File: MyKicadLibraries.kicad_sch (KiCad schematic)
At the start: 23 parts, among them J1 Conn_01x08, J2 Conn_01x08, J3 POGO Pins, J4 c8-inlet, J5 FTDI, J6 Micro_SD_Card, SW1 Schurter Switch, U1 radio-receiver, U10 rdm-6300, U11 magnetic-charger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

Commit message: Update tp4056 footprint
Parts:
- gave numbers to parts that had none: 1
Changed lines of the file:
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@@
   (symbol (lib_id "ftdi-connector:TTL") (at 126.746 53.848 0) (unit 1)
     (in_bom yes) (on_board yes) (fields_autoplaced)
-    (property "Reference" "U?" (id 0) (at 133.604 53.8479 0)
+    (property "Reference" "U13" (id 0) (at 133.604 53.8479 0)
       (effects (font (size 1.27 1.27)) (justify left))
     )
@@
     )
     (path "/435d2a60-6fae-43fe-9627-fd91fed8fe4a"
-      (reference "U?") (unit 1) (value "TTL") (footprint "Connector_PinHeader_2.54mm:PinHeader_1x04_P2.54mm_Vertical")
-    )
-  )
+      (reference "U13") (unit 1) (value "TTL") (footprint "Connector_PinHeader_2.54mm:PinHeader_1x04_P2.54mm_Vertical")
+    )
+  )

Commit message: Add SOIC8 breakout
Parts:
- added J7, J9: Conn_01x04, Connector_PinHeader_2.54mm:PinHeader_1x04_P2.54mm_Vertical, symbol Connector_Generic:Conn_01x04
- added J8: Conn_02x04_Counter_Clockwise, Package_SO:SOIC-8_3.9x4.9mm_P1.27mm, symbol Connector_Generic:Conn_02x04_Counter_Clockwise
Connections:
- new net: J8.5 (Pin_5), J9.1 (Pin_1)
- new net: J8.6 (Pin_6), J9.2 (Pin_2)
- new net: J8.7 (Pin_7), J9.3 (Pin_3)
- new net: J8.8 (Pin_8), J9.4 (Pin_4)
- new net: J7.1 (Pin_1), J8.1 (Pin_1)
- new net: J7.2 (Pin_2), J8.2 (Pin_2)
- new net: J7.3 (Pin_3), J8.3 (Pin_3)
- new net: J7.4 (Pin_4), J8.4 (Pin_4)
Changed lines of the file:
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@@
+    (pin "4")
+  )
+  (symbol (lib_id "Connector_Generic:Conn_01x04") (at 260.604 29.21 0) (mirror x) (unit 1)
+    (in_bom yes) (on_board yes) (fields_autoplaced)
+    (property "Reference" "J9" (id 0) (at 260.604 20.32 0))
+    (property "Value" "Conn_01x04" (id 1) (at 260.604 20.574 0)
+      (effects (font (size 1.27 1.27)) hide)
+    )
+    (property "Footprint" "Connector_PinHeader_2.54mm:PinHeader_1x04_P2.54mm_Vertical" (id 2) (at 260.604 29.21 0)
+      (effects (font (size 1.27 1.27)) hide)
+    )
+    (property "Datasheet" "~" (id 3) (at 260.604 29.21 0)
+      (effects (font (size 1.27 1.27)) hide)
+    )
+    (pin "1")
+    (pin "2")
+    (pin "3")
+    (pin "4")
+  )
+  (symbol (lib_id "Connector_Generic:Conn_01x04") (at 237.744 26.67 0) (mirror y) (unit 1)
+    (in_bom yes) (on_board yes) (fields_autoplaced)
+    (property "Reference" "J7" (id 0) (at 237.744 20.32 0))
+    (property "Value" "Conn_01x04" (id 1) (at 237.744 20.32 0)
+      (effects (font (size 1.27 1.27)) hide)
+    )
+    (property "Footprint" "Connector_PinHeader_2.54mm:PinHeader_1x04_P2.54mm_Vertical" (id 2) (at 237.744 26.67 0)
+      (effects (font (size 1.27 1.27)) hide)
+    )
+    (property "Datasheet" "~" (id 3) (at 237.744 26.67 0)
+      (effects (font (size 1.27 1.27)) hide)
+    )
+    (pin "1")
+    (pin "2")
+    (pin "3")
     (pin "4")
   )
@@
     (pin "9")
   )
+  (symbol (lib_id "Connector_Generic:Conn_02x04_Counter_Clockwise") (at 247.904 26.67 0) (unit 1)
+    (in_bom yes) (on_board yes) (fields_autoplaced)
+    (property "Reference" "J8" (id 0) (at 249.174 17.78 0))
+    (property "Value" "Conn_02x04_Counter_Clockwise" (id 1) (at 249.174 20.32 0))
+    (property "Footprint" "Package_SO:SOIC-8_3.9x4.9mm_P1.27mm" (id 2) (at 247.904 26.67 0)
+      (effects (font (size 1.27 1.27)) hide)
+    )
+    (property "Datasheet" "~" (id 3) (at 247.904 26.67 0)
+      (effects (font (size 1.27 1.27)) hide)
+    )
+    (pin "1")
+    (pin "2")
+    (pin "3")
+    (pin "4")
+    (pin "5")
+    (pin "6")
+    (pin "7")
+    (pin "8")
+  )
   (symbol (lib_id "ESP8266:ESP-12E") (at 240.665 135.255 0) (unit 1)
     (in_bom yes) (on_board yes) (fields_autoplaced)
@@
       (reference "J6") (unit 1) (value "Micro_SD_Card") (footprint "sd-card:sd-card")
     )
+    (path "/c7e9b8b9-307f-4e5a-a9a6-364a90b8e346"
+      (reference "J7") (unit 1) (value "Conn_01x04") (footprint "Connector_PinHeader_2.54mm:PinHeader_1x04_P2.54mm_Vertical")
+    )
+    (path "/d1d3df4c-041c-4333-92a6-361f8f8487b4"
+      (reference "J8") (unit 1) (value "Conn_02x04_Counter_Clockwise") (footprint "Package_SO:SOIC-8_3.9x4.9mm_P1.27mm")
+    )
+    (path "/c112f6ba-1a8d-4939-9e1a-222f084633ca"
+      (reference "J9") (unit 1) (value "Conn_01x04") (footprint "Connector_PinHeader_2.54mm:PinHeader_1x04_P2.54mm_Vertical")
+    )
     (path "/93625391-d5f1-4afc-86f7-69a3da3b5437"

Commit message: Add rcj-22 plug as well as lxb18 module
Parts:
- added J10: RCJ-22, rcj-22:rcj-22, symbol rcj-22:RCJ-22
- added U14: lxb18, lxb18:lxb18, symbol lxb18:lxb18
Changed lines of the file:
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@@
     (pin "7")
+  )
+  (symbol (lib_id "rcj-22:RCJ-22") (at 164.592 132.08 0) (unit 1)
+    (in_bom yes) (on_board yes) (fields_autoplaced)
+    (property "Reference" "J10" (id 0) (at 163.0045 121.92 0))
+    (property "Value" "RCJ-22" (id 1) (at 163.0045 124.46 0))
+    (property "Footprint" "rcj-22:rcj-22" (id 2) (at 162.687 140.97 0)
+      (effects (font (size 1.27 1.27)) (justify bottom) hide)
+    )
+    (property "Datasheet" "" (id 3) (at 179.832 142.24 0)
+      (effects (font (size 1.27 1.27)) hide)
+    )
+    (pin "1")
+    (pin "2")
+    (pin "3")
   )
   (symbol (lib_id "adafruit-MAX98357:adafruit-MAX98357") (at 94.234 116.586 0) (unit 1)
@@
     (pin "1")
     (pin "2")
+  )
+  (symbol (lib_id "lxb18:lxb18") (at 247.396 75.438 0) (unit 1)
+    (in_bom yes) (on_board yes)
+    (property "Reference" "U14" (id 0) (at 240.03 66.548 0)
+      (effects (font (size 1.27 1.27)) (justify left))
+    )
+    (property "Value" "lxb18" (id 1) (at 250.698 84.328 0)
+      (effects (font (size 1.27 1.27)) (justify left))
+    )
+    (property "Footprint" "lxb18:lxb18" (id 2) (at 242.316 75.438 0)
+      (effects (font (size 1.27 1.27)) hide)
+    )
+    (property "Datasheet" "" (id 3) (at 242.316 75.438 0)
+      (effects (font (size 1.27 1.27)) hide)
+    )
+    (pin "1")
+    (pin "2")
+    (pin "3")
+    (pin "4")
+    (pin "5")
+    (pin "6")
+    (pin "7")
+    (pin "8")
   )
   (symbol (lib_id "c8-inlet:c8-inlet") (at 94.234 77.978 0) (unit 1)
@@
       (reference "J9") (unit 1) (value "Conn_01x04") (footprint "Connector_PinHeader_2.54mm:PinHeader_1x04_P2.54mm_Vertical")
     )
+    (path "/4e8a5cd3-7bbd-43a2-b3b1-8113fc79bbd5"
+      (reference "J10") (unit 1) (value "RCJ-22") (footprint "rcj-22:rcj-22")
+    )
     (path "/93625391-d5f1-4afc-86f7-69a3da3b5437"
       (reference "LIN1") (unit 1) (value "LEDs_In") (footprint "neopixel-strip:neopixel-strip")
@@
       (reference "U13") (unit 1) (value "TTL") (footprint "Connector_PinHeader_2.54mm:PinHeader_1x04_P2.54mm_Vertical")
     )
-  )
+    (path "/6cf58933-bb3e-42e1-bf60-7634f8d5f4b4"
+      (reference "U14") (unit 1) (value "lxb18") (footprint "lxb18:lxb18")
+    )
+  )

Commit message: Add midi connector
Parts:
- added J11: DIN-5, midi:midi, symbol Connector:DIN-5
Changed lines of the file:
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@@
     (pin "2")
+  )
+  (symbol (lib_id "Connector:DIN-5") (at 158.75 97.79 0) (unit 1)
+    (in_bom yes) (on_board yes) (fields_autoplaced)
+    (property "Reference" "J11" (id 0) (at 158.7501 105.41 0))
+    (property "Value" "DIN-5" (id 1) (at 158.7501 107.95 0))
+    (property "Footprint" "midi:midi" (id 2) (at 158.75 97.79 0)
+      (effects (font (size 1.27 1.27)) hide)
+    )
+    (property "Datasheet" "http://www.mouser.com/ds/2/18/40_c091_abd_e-75918.pdf" (id 3) (at 158.75 97.79 0)
+      (effects (font (size 1.27 1.27)) hide)
+    )
+    (pin "1")
+    (pin "2")
+    (pin "3")
+    (pin "4")
+    (pin "5")
   )
   (symbol (lib_id "ftdi-connector:FTDI") (at 108.204 54.61 0) (unit 1)
@@
       (reference "J10") (unit 1) (value "RCJ-22") (footprint "rcj-22:rcj-22")
     )
+    (path "/13dd7a5b-3ad4-40e9-9df7-e158c8bd37e9"
+      (reference "J11") (unit 1) (value "DIN-5") (footprint "midi:midi")
+    )
     (path "/93625391-d5f1-4afc-86f7-69a3da3b5437"

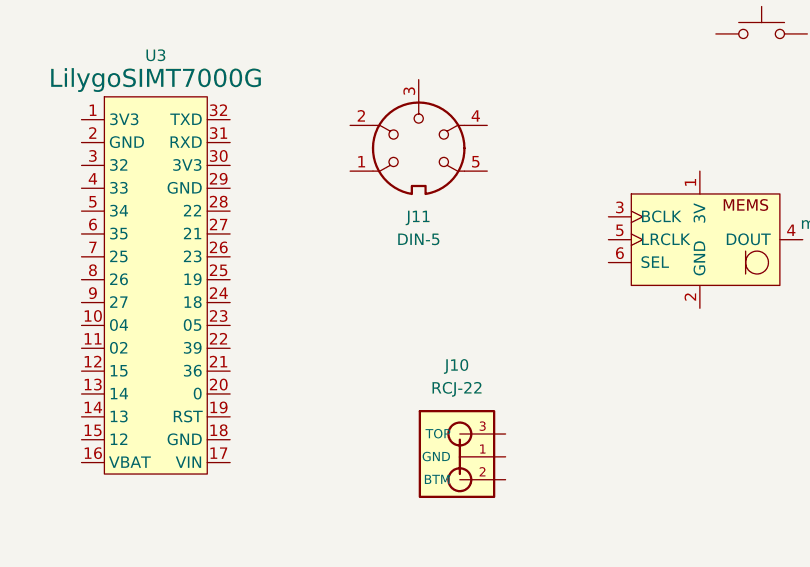
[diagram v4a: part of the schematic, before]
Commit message: Add din6 midi plug
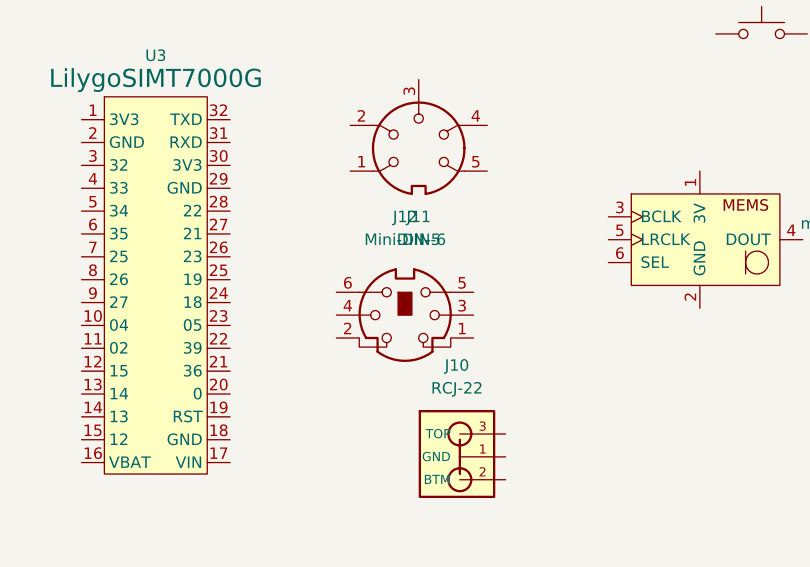
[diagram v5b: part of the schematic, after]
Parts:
- added J12: Mini-DIN-6, midi:midi-din6, symbol Connector:Mini-DIN-6
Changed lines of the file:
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@@
     (pin "THERMAL")
+  )
+  (symbol (lib_id "Connector:Mini-DIN-6") (at 157.226 116.332 0) (unit 1)
+    (in_bom yes) (on_board yes) (fields_autoplaced)
+    (property "Reference" "J12" (id 0) (at 157.2437 105.41 0))
+    (property "Value" "Mini-DIN-6" (id 1) (at 157.2437 107.95 0))
+    (property "Footprint" "midi:midi-din6" (id 2) (at 157.226 116.332 0)
+      (effects (font (size 1.27 1.27)) hide)
+    )
+    (property "Datasheet" "http://service.powerdynamics.com/ec/Catalog17/Section%2011.pdf" (id 3) (at 157.226 116.332 0)
+      (effects (font (size 1.27 1.27)) hide)
+    )
+    (pin "1")
+    (pin "2")
+    (pin "3")
+    (pin "4")
+    (pin "5")
+    (pin "6")
   )
   (symbol (lib_id "Switch:SW_Push") (at 196.85 85.09 0) (unit 1)
@@
       (reference "J11") (unit 1) (value "DIN-5") (footprint "midi:midi")
     )
+    (path "/62ed3167-06a5-430d-adba-50010e067d40"
+      (reference "J12") (unit 1) (value "Mini-DIN-6") (footprint "midi:midi-din6")
+    )
     (path "/93625391-d5f1-4afc-86f7-69a3da3b5437"

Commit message: Update submodules
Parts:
- added U15: esp32-wemos-d1-mini, esp32-wemos-d1-mini:esp32-wemos-d1-mini, symbol esp32-wemos-d1-mini:esp32-wemos-d1-mini
- added U16: TCRT5000, tcrt5000:tcrt5000, symbol tcrt5000:TCRT5000
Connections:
- net at U12.7 (LRC): no longer U12.8 (VDD)
- now unconnected: U12.3 (GND)

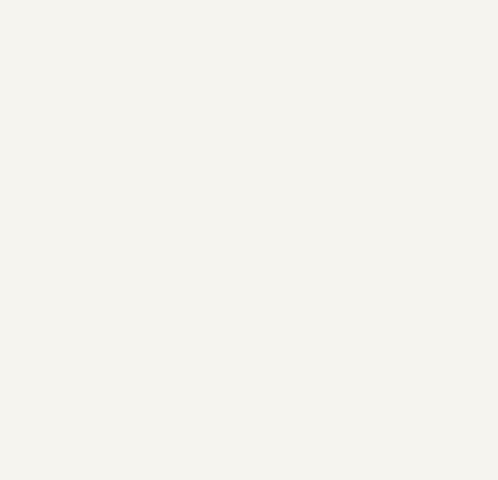
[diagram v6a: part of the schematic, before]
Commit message: Add USB pcb trace footprint
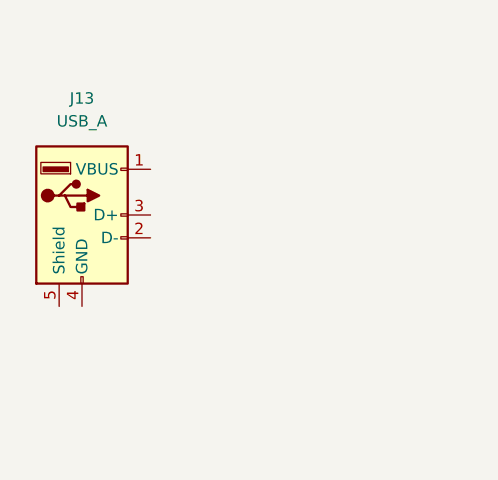
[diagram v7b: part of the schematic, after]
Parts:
- added J13: USB_A, usb-a-pcb:usb-a-pcb, symbol Connector:USB_A
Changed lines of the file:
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@@
+    (pin "5")
+  )
+  (symbol (lib_id "Connector:USB_A") (at -27.94 35.814 0) (unit 1)
+    (in_bom yes) (on_board yes) (fields_autoplaced)
+    (property "Reference" "J13" (id 0) (at -27.94 22.86 0))
+    (property "Value" "USB_A" (id 1) (at -27.94 25.4 0))
+    (property "Footprint" "usb-a-pcb:usb-a-pcb" (id 2) (at -24.13 37.084 0)
+      (effects (font (size 1.27 1.27)) hide)
+    )
+    (property "Datasheet" " ~" (id 3) (at -24.13 37.084 0)
+      (effects (font (size 1.27 1.27)) hide)
+    )
+    (pin "1")
+    (pin "2")
+    (pin "3")
+    (pin "4")
     (pin "5")
   )
@@
       (reference "J12") (unit 1) (value "Mini-DIN-6") (footprint "midi:midi-din6")
     )
+    (path "/18165b05-bcd3-4516-9a0b-bbd618d69253"
+      (reference "J13") (unit 1) (value "USB_A") (footprint "usb-a-pcb:usb-a-pcb")
+    )
     (path "/93625391-d5f1-4afc-86f7-69a3da3b5437"

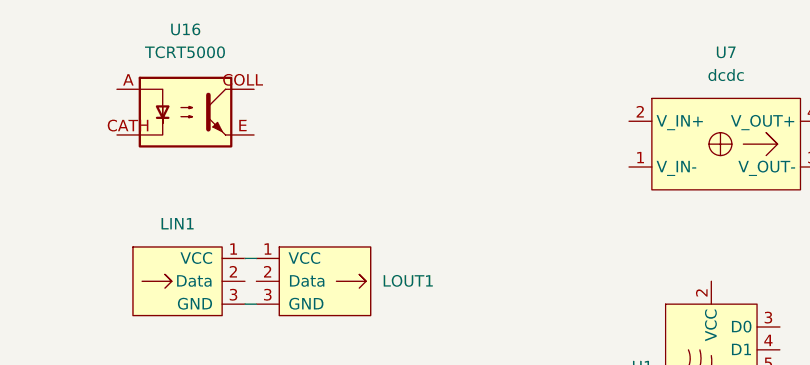
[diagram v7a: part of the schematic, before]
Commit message: Add OPB607A IR module
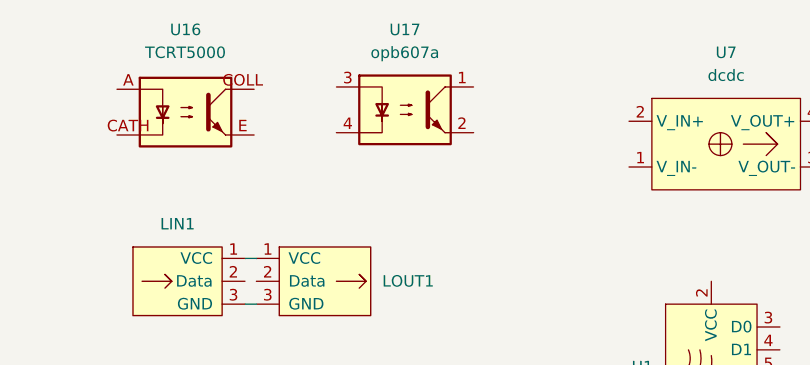
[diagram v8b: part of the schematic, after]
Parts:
- added U17: opb607a, opb607a:opb607a, symbol opb607a:opb607a
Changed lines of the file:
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@@
     (pin "3")
+  )
+  (symbol (lib_id "opb607a:opb607a") (at 54.61 24.13 0) (unit 1)
+    (in_bom yes) (on_board yes) (fields_autoplaced)
+    (property "Reference" "U17" (id 0) (at 54.61 15.24 0))
+    (property "Value" "opb607a" (id 1) (at 54.61 17.78 0))
+    (property "Footprint" "opb607a:opb607a" (id 2) (at 54.61 32.385 0)
+      (effects (font (size 1.27 1.27)) hide)
+    )
+    (property "Datasheet" "https://www.ttelectronics.com/TTElectronics/media/ProductFiles/Datasheet/OPB606-607.pdf" (id 3) (at 53.34 34.29 0)
+      (effects (font (size 1.27 1.27)) hide)
+    )
+    (pin "1")
+    (pin "2")
+    (pin "3")
+    (pin "4")
   )
   (symbol (lib_id "adafruit-MAX98357:adafruit-MAX98357") (at 94.234 116.586 0) (unit 1)
@@
       (reference "U16") (unit 1) (value "TCRT5000") (footprint "tcrt5000:tcrt5000")
     )
-  )
+    (path "/562dbfaa-6384-41db-8c52-ec0fea9b4fdf"
+      (reference "U17") (unit 1) (value "opb607a") (footprint "opb607a:opb607a")
+    )
+  )
